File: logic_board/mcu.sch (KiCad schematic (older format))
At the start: 15 parts, among them J1 SWD, J6 Serial, SW1 TL3315NF160Q, SW2 TL3315NF160Q, SW3 TL3315NF160Q, SW4 TL3315NF160Q, U1 STM32G474CET6, Y1 8 MHz

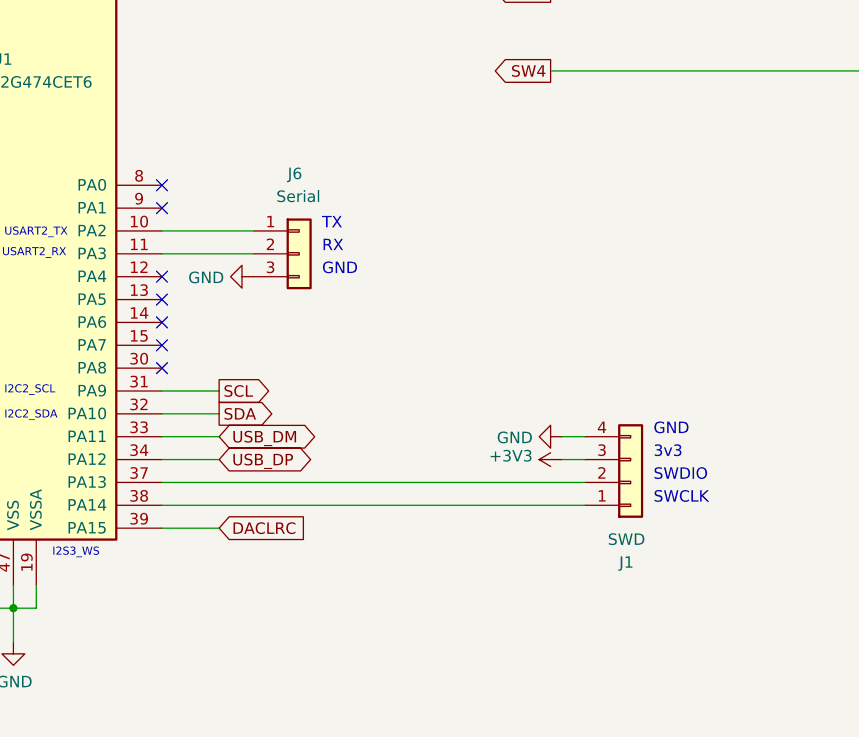
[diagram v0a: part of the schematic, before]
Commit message: Consolidate UART and SWD headers into a single one, which takes up less space.
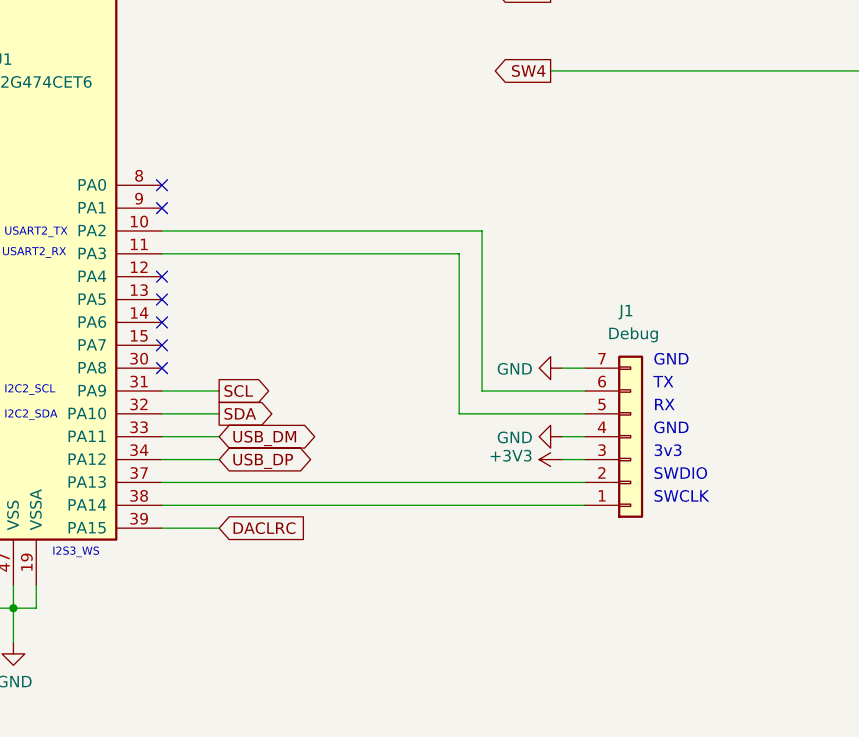
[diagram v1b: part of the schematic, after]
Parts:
- removed J1: SWD, Pin_Headers:Pin_Header_Straight_1x04_Pitch2.54mm, symbol Connector_Generic:Conn_01x04
- removed J6: Serial, Pin_Headers:Pin_Header_Straight_1x03_Pitch2.54mm, symbol Connector_Generic:Conn_01x03
- added J1: Debug, Pin_Headers:Pin_Header_Straight_1x07_Pitch2.54mm, symbol Connector_Generic:Conn_01x07
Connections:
- net +3V3: now also J1.3 (Pin_3)
- net GND: now also J1.4 (Pin_4), J1.7 (Pin_7)
- net at U1.10 (PA2): now also J1.6 (Pin_6)
- net at U1.11 (PA3): now also J1.5 (Pin_5)
- net at U1.37 (PA13): now also J1.2 (Pin_2)
- net at U1.38 (PA14): now also J1.1 (Pin_1)
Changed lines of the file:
@@
 Text GLabel 4550 3250 0    50   Input ~ 0
 SW4
-$Comp
-L Connector_Generic:Conn_01x04 J1
-U 1 1 5E4DEDD9
-P 8200 4900
-F 0 "J1" H 8150 5250 50  0000 L CNN
-F 1 "SWD" H 8100 5150 50  0000 L CNN
-F 2 "Pin_Headers:Pin_Header_Straight_1x04_Pitch2.54mm" H 8200 4900 50  0001 C CNN
-F 3 "~" H 8200 4900 50  0001 C CNN
-	1    8200 4900
-	1    0    0    1
-$EndComp
 Text Notes 8300 4900 0    50   ~ 0
 SWDIO
@@
 	1    0    0    -1
 $EndComp
-$Comp
-L Connector_Generic:Conn_01x03 J6
-U 1 1 5E57B910
-P 6750 3900
-F 0 "J6" H 6700 4250 50  0000 L CNN
-F 1 "Serial" H 6650 4150 50  0000 L CNN
-F 2 "Pin_Headers:Pin_Header_Straight_1x03_Pitch2.54mm" H 6750 3900 50  0001 C CNN
-F 3 "~" H 6750 3900 50  0001 C CNN
-	1    6750 3900
-	1    0    0    -1
-$EndComp
-Wire Wire Line
-	6150 3800 6550 3800
-Wire Wire Line
-	6150 3900 6550 3900
-$Comp
-L power:GND #PWR0106
-U 1 1 5E58AEDF
-P 6550 4000
-F 0 "#PWR0106" H 6550 3750 50  0001 C CNN
-F 1 "GND" V 6555 3872 50  0000 R CNN
-F 2 "" H 6550 4000 50  0001 C CNN
-F 3 "" H 6550 4000 50  0001 C CNN
-	1    6550 4000
-	0    1    1    0
-$EndComp
 Text Notes 8300 5000 0    50   ~ 0
 SWCLK
@@
 Text Notes 8300 4700 0    50   ~ 0
 GND
-Text Notes 6850 3800 0    50   ~ 0
+Text Notes 8300 4500 0    50   ~ 0
 TX
-Text Notes 6850 3900 0    50   ~ 0
+Text Notes 8300 4600 0    50   ~ 0
 RX
-Text Notes 6850 4000 0    50   ~ 0
+Text Notes 8300 4400 0    50   ~ 0
 GND
 Wire Wire Line
@@
 	6150 4600 6400 4600
 NoConn ~ 6150 4400
+$Comp
+L Connector_Generic:Conn_01x07 J1
+U 1 1 5E41669C
+P 8200 4700
+F 0 "J1" H 8150 4150 50  0000 L CNN
+F 1 "Debug" H 8100 4250 50  0000 L CNN
+F 2 "Pin_Headers:Pin_Header_Straight_1x07_Pitch2.54mm" H 8200 4700 50  0001 C CNN
+F 3 "~" H 8200 4700 50  0001 C CNN
+	1    8200 4700
+	1    0    0    1
+$EndComp
+Wire Wire Line
+	6150 3900 7450 3900
+$Comp
+L power:GND #PWR011
+U 1 1 5E42451A
+P 7900 4400
+F 0 "#PWR011" H 7900 4150 50  0001 C CNN
+F 1 "GND" V 7905 4272 50  0000 R CNN
+F 2 "" H 7900 4400 50  0001 C CNN
+F 3 "" H 7900 4400 50  0001 C CNN
+	1    7900 4400
+	0    1    1    0
+$EndComp
+Wire Wire Line
+	7900 4400 8000 4400
+Wire Wire Line
+	7450 4600 8000 4600
+Wire Wire Line
+	7450 3900 7450 4600
+Wire Wire Line
+	8000 4500 7550 4500
+Wire Wire Line
+	7550 4500 7550 3800
+Wire Wire Line
+	6150 3800 7550 3800
 $EndSCHEMATC

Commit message: Update to symbols from newest KiCad
LEDs were also on the wrong side of the board.
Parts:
- C4: footprint Capacitors_SMD:C_0805_HandSoldering -> Capacitor_SMD:C_0805_2012Metric_Pad1.15x1.40mm_HandSolder
- C5, C6, C7, C8: footprint Capacitors_SMD:C_0402 -> Capacitor_SMD:C_0402_1005Metric
- D3: footprint LEDs:LED_0603_HandSoldering -> LED_SMD:LED_0603_1608Metric_Pad1.05x0.95mm_HandSolder
- J1: footprint Pin_Headers:Pin_Header_Straight_1x07_Pitch2.54mm -> Connector_PinHeader_2.54mm:PinHeader_1x07_P2.54mm_Vertical
- R18: footprint Resistors_SMD:R_0402 -> Resistor_SMD:R_0402_1005Metric
- U1: footprint Housings_QFP:LQFP-48_7x7mm_Pitch0.5mm -> Package_QFP:LQFP-48_7x7mm_P0.5mm
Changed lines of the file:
@@
 F 0 "C4" H 2818 6446 50  0000 L CNN
 F 1 "10uF" H 2818 6355 50  0000 L CNN
-F 2 "Capacitors_SMD:C_0805_HandSoldering" H 2738 6250 50  0001 C CNN
+F 2 "Capacitor_SMD:C_0805_2012Metric_Pad1.15x1.40mm_HandSolder" H 2738 6250 50  0001 C CNN
 F 3 "~" H 2700 6400 50  0001 C CNN
 	1    2700 6400
@@
 F 0 "C5" H 3165 6446 50  0000 L CNN
 F 1 "0.1uF" H 3165 6355 50  0000 L CNN
-F 2 "Capacitors_SMD:C_0402" H 3088 6250 50  0001 C CNN
+F 2 "Capacitor_SMD:C_0402_1005Metric" H 3088 6250 50  0001 C CNN
 F 3 "~" H 3050 6400 50  0001 C CNN
 	1    3050 6400
@@
 F 0 "C6" H 3465 6446 50  0000 L CNN
 F 1 "0.1uF" H 3465 6355 50  0000 L CNN
-F 2 "Capacitors_SMD:C_0402" H 3388 6250 50  0001 C CNN
+F 2 "Capacitor_SMD:C_0402_1005Metric" H 3388 6250 50  0001 C CNN
 F 3 "~" H 3350 6400 50  0001 C CNN
 	1    3350 6400
@@
 F 0 "C7" H 3815 6446 50  0000 L CNN
 F 1 "0.1uF" H 3815 6355 50  0000 L CNN
-F 2 "Capacitors_SMD:C_0402" H 3738 6250 50  0001 C CNN
+F 2 "Capacitor_SMD:C_0402_1005Metric" H 3738 6250 50  0001 C CNN
 F 3 "~" H 3700 6400 50  0001 C CNN
 	1    3700 6400
@@
 F 0 "C8" H 4165 6446 50  0000 L CNN
 F 1 "0.1uF" H 4165 6355 50  0000 L CNN
-F 2 "Capacitors_SMD:C_0402" H 4088 6250 50  0001 C CNN
+F 2 "Capacitor_SMD:C_0402_1005Metric" H 4088 6250 50  0001 C CNN
 F 3 "~" H 4050 6400 50  0001 C CNN
 	1    4050 6400
@@
 F 0 "U1" H 5450 3250 50  0000 C CNN
 F 1 "STM32G474CET6" H 5550 3150 50  0000 C CNN
-F 2 "Housings_QFP:LQFP-48_7x7mm_Pitch0.5mm" H 5400 3150 50  0001 C CNN
+F 2 "Package_QFP:LQFP-48_7x7mm_P0.5mm" H 5400 3150 50  0001 C CNN
 F 3 "https://www.st.com/resource/en/datasheet/stm32g473cb.pdf" H 5400 3150 50  0001 C CNN
 	1    5400 3150
@@
 F 0 "D3" H 3943 4916 50  0000 C CNN
 F 1 "Debug" H 3943 4825 50  0000 C CNN
-F 2 "LEDs:LED_0603_HandSoldering" H 3950 4700 50  0001 C CNN
+F 2 "LED_SMD:LED_0603_1608Metric_Pad1.05x0.95mm_HandSolder" H 3950 4700 50  0001 C CNN
 F 3 "~" H 3950 4700 50  0001 C CNN
 	1    3950 4700
@@
 F 0 "R18" V 3293 4700 50  0000 C CNN
 F 1 "1.5k" V 3384 4700 50  0000 C CNN
-F 2 "Resistors_SMD:R_0402" V 3430 4700 50  0001 C CNN
+F 2 "Resistor_SMD:R_0402_1005Metric" V 3430 4700 50  0001 C CNN
 F 3 "~" H 3500 4700 50  0001 C CNN
 	1    3500 4700
@@
 F 0 "J1" H 8150 4150 50  0000 L CNN
 F 1 "Debug" H 8100 4250 50  0000 L CNN
-F 2 "Pin_Headers:Pin_Header_Straight_1x07_Pitch2.54mm" H 8200 4700 50  0001 C CNN
+F 2 "Connector_PinHeader_2.54mm:PinHeader_1x07_P2.54mm_Vertical" H 8200 4700 50  0001 C CNN
 F 3 "~" H 8200 4700 50  0001 C CNN
 	1    8200 4700

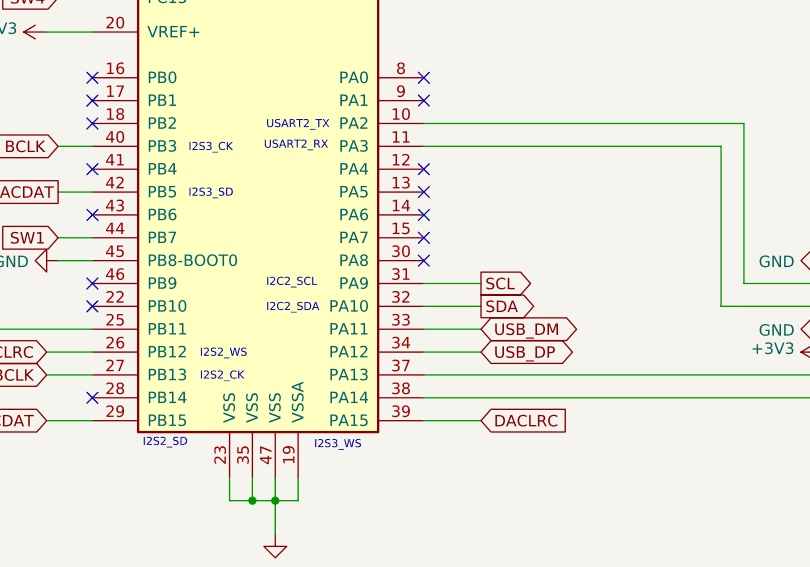
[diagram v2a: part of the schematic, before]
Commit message: Fix I2C2_SDA, which was mislabeled in the STM32G473 datasheet.
It now connects to pin30. In the G474 datasheet, both places
that reference this pin agree.
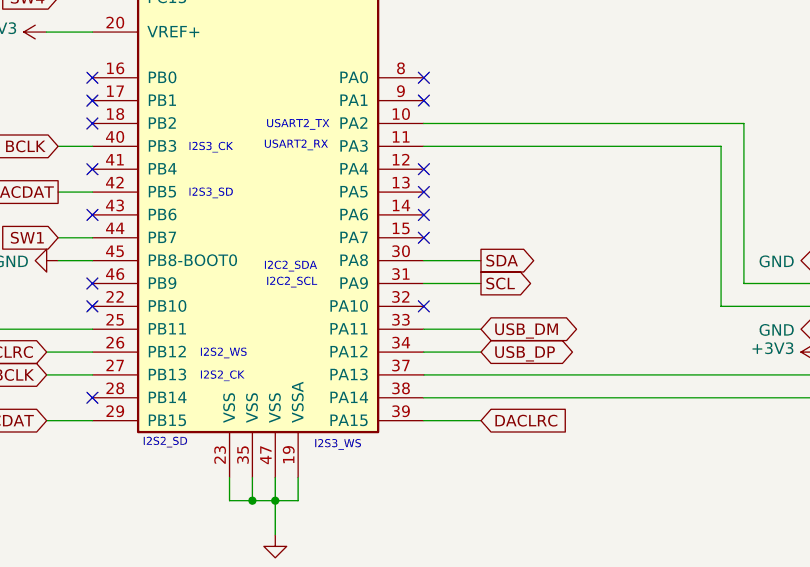
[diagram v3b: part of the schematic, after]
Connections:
- net SDA: now also U1.30 (PA8); no longer U1.32 (PA10)
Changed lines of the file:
@@
 Wire Wire Line
 	4550 4300 4700 4300
-Text GLabel 6400 4600 2    50   Output ~ 0
+Text GLabel 6400 4400 2    50   Output ~ 0
 SDA
 Text GLabel 6400 4500 2    50   Output ~ 0
@@
 Text Notes 5450 3920 0    35   ~ 0
 USART2_RX
-Text Notes 5460 4630 0    35   ~ 0
+Text Notes 5450 4450 0    35   ~ 0
 I2C2_SDA
 Text Notes 5460 4520 0    35   ~ 0
@@
 OSC_OUT
 Wire Wire Line
-	6150 4600 6400 4600
-NoConn ~ 6150 4400
+	6150 4400 6400 4400
+NoConn ~ 6150 4600
 $Comp
 L Connector_Generic:Conn_01x07 J1

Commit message: Use through-hole USB C connector for easier soldering.
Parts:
- C6, C8: footprint Capacitor_SMD:C_0402_1005Metric -> Capacitor_SMD:C_0603_1608Metric_Pad1.05x0.95mm_HandSolder
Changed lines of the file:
@@
 F 0 "C6" H 3465 6446 50  0000 L CNN
 F 1 "0.1uF" H 3465 6355 50  0000 L CNN
-F 2 "Capacitor_SMD:C_0402_1005Metric" H 3388 6250 50  0001 C CNN
+F 2 "Capacitor_SMD:C_0603_1608Metric_Pad1.05x0.95mm_HandSolder" H 3388 6250 50  0001 C CNN
 F 3 "~" H 3350 6400 50  0001 C CNN
 	1    3350 6400
@@
 F 0 "C8" H 4165 6446 50  0000 L CNN
 F 1 "0.1uF" H 4165 6355 50  0000 L CNN
-F 2 "Capacitor_SMD:C_0402_1005Metric" H 4088 6250 50  0001 C CNN
+F 2 "Capacitor_SMD:C_0603_1608Metric_Pad1.05x0.95mm_HandSolder" H 4088 6250 50  0001 C CNN
 F 3 "~" H 4050 6400 50  0001 C CNN
 	1    4050 6400

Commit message: Update all 0402 SMD packages to 0603
Mainly to make soldering easier. 0402 was unnecessarily small.
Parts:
- C5, C7: footprint Capacitor_SMD:C_0402_1005Metric -> Capacitor_SMD:C_0603_1608Metric_Pad1.05x0.95mm_HandSolder
- R18: footprint Resistor_SMD:R_0402_1005Metric -> Resistor_SMD:R_0603_1608Metric_Pad1.05x0.95mm_HandSolder
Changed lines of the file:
@@
 F 0 "C5" H 3165 6446 50  0000 L CNN
 F 1 "0.1uF" H 3165 6355 50  0000 L CNN
-F 2 "Capacitor_SMD:C_0402_1005Metric" H 3088 6250 50  0001 C CNN
+F 2 "Capacitor_SMD:C_0603_1608Metric_Pad1.05x0.95mm_HandSolder" H 3088 6250 50  0001 C CNN
 F 3 "~" H 3050 6400 50  0001 C CNN
 	1    3050 6400
@@
 F 0 "C7" H 3815 6446 50  0000 L CNN
 F 1 "0.1uF" H 3815 6355 50  0000 L CNN
-F 2 "Capacitor_SMD:C_0402_1005Metric" H 3738 6250 50  0001 C CNN
+F 2 "Capacitor_SMD:C_0603_1608Metric_Pad1.05x0.95mm_HandSolder" H 3738 6250 50  0001 C CNN
 F 3 "~" H 3700 6400 50  0001 C CNN
 	1    3700 6400
@@
 F 0 "R18" V 3293 4700 50  0000 C CNN
 F 1 "1.5k" V 3384 4700 50  0000 C CNN
-F 2 "Resistor_SMD:R_0402_1005Metric" V 3430 4700 50  0001 C CNN
+F 2 "Resistor_SMD:R_0603_1608Metric_Pad1.05x0.95mm_HandSolder" V 3430 4700 50  0001 C CNN
 F 3 "~" H 3500 4700 50  0001 C CNN
 	1    3500 4700
